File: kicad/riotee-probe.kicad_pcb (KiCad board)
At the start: 2 copper layers, 43.2 x 22.9 mm, 70 parts, among them J1 12402012E212A, J2 Conn_01x05, J3 Conn_02x05_Odd_Even, J4 Conn_01x05, U1 RP2040, U2 W25Q16JVUXIQ, U3 74LVC2T45GT, U4 74LVC2T45GT, U5 74LVC2T45GT, U6 74LVC2T45GT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

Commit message: adjust values of level translator series resistors
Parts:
- R10, R11, R12, R13, R14, R15, R20, R21, R23, R24: value 120R -> 12R
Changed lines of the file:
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@@
       (effects (font (size 1 1) (thickness 0.15)))
     )
-    (fp_text value "120R" (at 0 1.17) (layer "F.Fab") hide
+    (fp_text value "12R" (at 0 1.17) (layer "F.Fab") hide
       (effects (font (size 1 1) (thickness 0.15)))
     )
@@
       (effects (font (size 1 1) (thickness 0.15)))
     )
-    (fp_text value "120R" (at 0 1.17) (layer "F.Fab") hide
+    (fp_text value "12R" (at 0 1.17) (layer "F.Fab") hide
       (effects (font (size 1 1) (thickness 0.15)))
     )
@@
       (effects (font (size 1 1) (thickness 0.15)))
     )
-    (fp_text value "120R" (at 0 1.17) (layer "F.Fab") hide
+    (fp_text value "12R" (at 0 1.17) (layer "F.Fab") hide
       (effects (font (size 1 1) (thickness 0.15)))
     )
@@
       (effects (font (size 1 1) (thickness 0.15)))
     )
-    (fp_text value "120R" (at 0 1.17) (layer "F.Fab") hide
+    (fp_text value "12R" (at 0 1.17) (layer "F.Fab") hide
       (effects (font (size 1 1) (thickness 0.15)))
     )
@@
       (effects (font (size 1 1) (thickness 0.15)))
     )
-    (fp_text value "120R" (at 0 1.17) (layer "F.Fab") hide
+    (fp_text value "12R" (at 0 1.17) (layer "F.Fab") hide
       (effects (font (size 1 1) (thickness 0.15)))
     )
@@
       (effects (font (size 1 1) (thickness 0.15)))
     )
-    (fp_text value "120R" (at 0 1.17) (layer "F.Fab") hide
+    (fp_text value "12R" (at 0 1.17) (layer "F.Fab") hide
       (effects (font (size 1 1) (thickness 0.15)))
     )
@@
       (effects (font (size 1 1) (thickness 0.15)))
     )
-    (fp_text value "120R" (at 0 1.17 90) (layer "F.Fab") hide
+    (fp_text value "12R" (at 0 1.17 90) (layer "F.Fab") hide
       (effects (font (size 1 1) (thickness 0.15)))
     )
@@
       (effects (font (size 1 1) (thickness 0.15)))
     )
-    (fp_text value "120R" (at 0 1.17) (layer "F.Fab") hide
+    (fp_text value "12R" (at 0 1.17) (layer "F.Fab") hide
       (effects (font (size 1 1) (thickness 0.15)))
     )
@@
       (effects (font (size 1 1) (thickness 0.15)))
     )
-    (fp_text value "120R" (at 0 1.17) (layer "F.Fab") hide
+    (fp_text value "12R" (at 0 1.17) (layer "F.Fab") hide
       (effects (font (size 1 1) (thickness 0.15)))
     )
@@
       (effects (font (size 1 1) (thickness 0.15)))
     )
-    (fp_text value "120R" (at 0 1.17) (layer "F.Fab") hide
+    (fp_text value "12R" (at 0 1.17) (layer "F.Fab") hide
       (effects (font (size 1 1) (thickness 0.15)))
     )

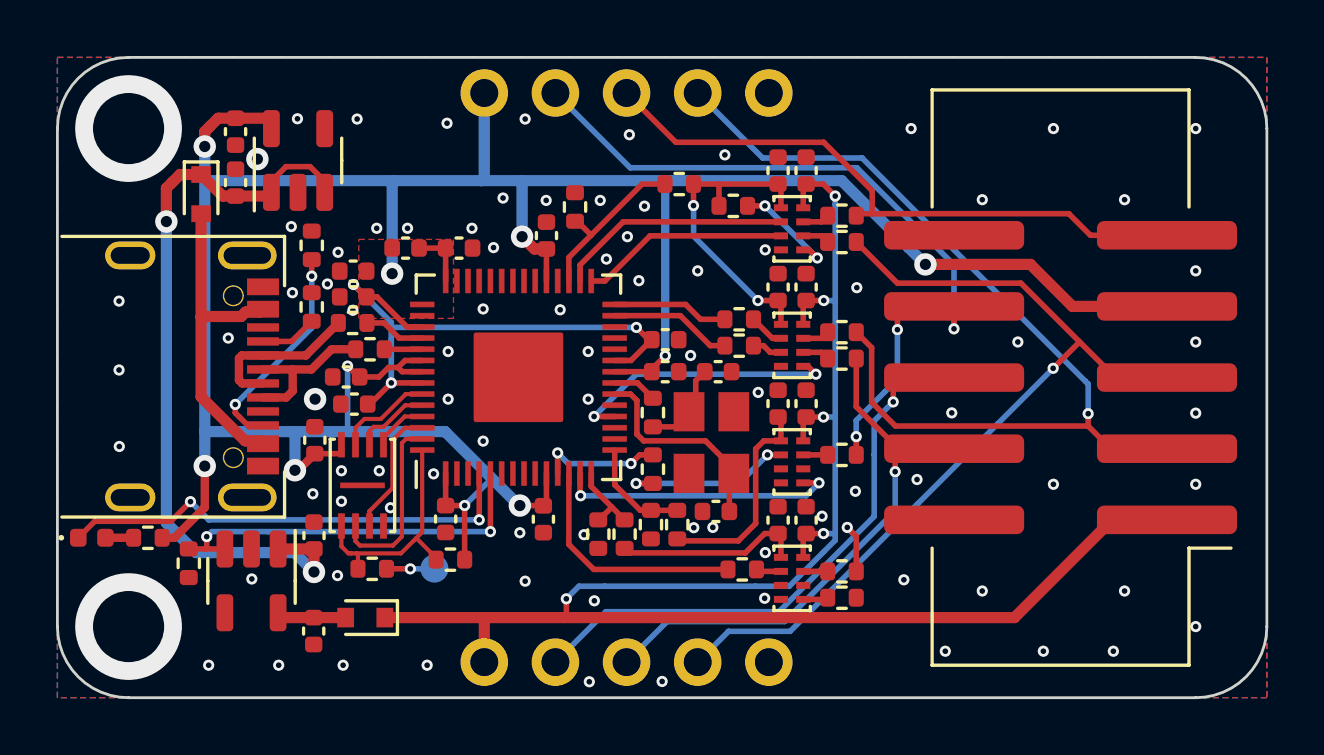
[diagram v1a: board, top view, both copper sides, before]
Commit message: replace target supply diode with analog switch
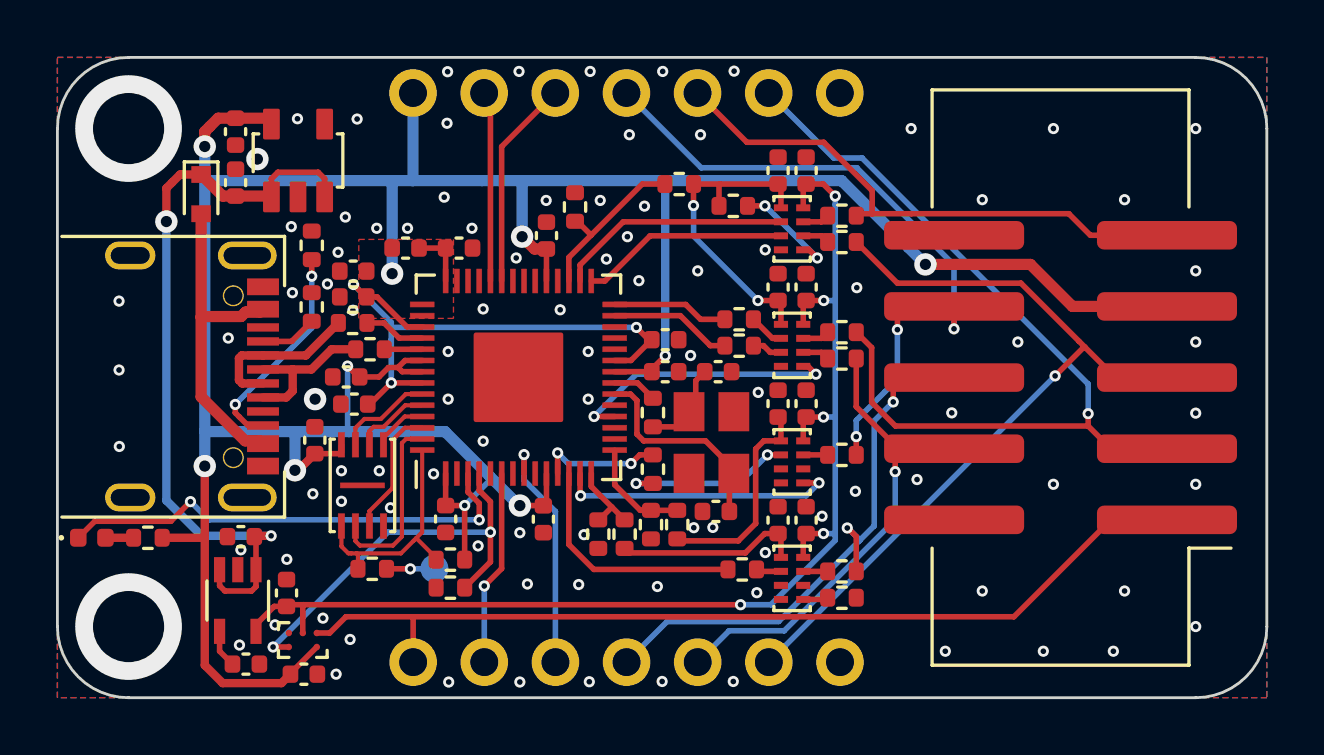
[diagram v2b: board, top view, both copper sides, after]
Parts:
- removed D3: D_Schottky, Diode_SMD:D_SOD-523
- added C25: DNP, Capacitor_SMD:C_0402_1005Metric, F.Cu at (184.5, 72.5)
- added C28: 0.1u, Capacitor_SMD:C_0402_1005Metric, F.Cu at (186.6, 72.8)
- added U9: TS5A3166YZP, riotee:TI_YZP0005, F.Cu at (186.6, 71.6)
- J2, J4: value Conn_01x05 -> Conn_01x07; footprint riotee:PinHeader_1x05_P2.54mm_Plain -> riotee:PinHeader_1x07_P2.54mm_Plain
- R27: value 5.1k -> 12R
- U7: value TLV73325PDBV -> TPS71721DCK; footprint Package_TO_SOT_SMD:SOT-23-5 -> riotee:TI_DCK0005A
- U8: footprint Package_TO_SOT_SMD:SOT-23-5 -> riotee:TI_DBV0005A
- moved R27 9.38 mm to (191.8, 69.7), turned to 0 degrees
- moved C23 2.61 mm to (184.3, 67.9), turned to 180 degrees
- moved J4 2.54 mm to (190.5, 52.1)
- moved J2 2.54 mm to (190.5, 72.4)
- moved C27 1.67 mm to (186.0, 69.9), turned to 90 degrees
- moved U7 0.85 mm to (184.2, 70.2)
- renumbered C25 to C27
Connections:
- C17 pad 1: /Connectors/TargetVcc -> +2V1
- C18 pad 1: /Connectors/TargetVcc -> +2V1
- C21 pad 1: /Connectors/TargetVcc -> +2V1
- C22 pad 1: /Connectors/TargetVcc -> +2V1
- C27 pad 1: Net-(C25-Pad1) -> +2V1
- J2 pad 2: /Connectors/Target_UART_TX -> /Connectors/PiGpio0
- J2 pad 3: /Connectors/Target_SWD.IO -> /Connectors/PiGpio1
- J2 pad 4: /Connectors/Target_SWD.CLK -> /Connectors/Target_UART_TX
- J2 pad 5: GND -> /Connectors/Target_SWD.IO
- J4 pad 2: /Connectors/Target_UART_RX -> /Connectors/PiGpio3
- J4 pad 3: /Connectors/Target_SBW.CLK -> /Connectors/PiGpio2
- J4 pad 4: /Connectors/Target_SBW.IO -> /Connectors/Target_UART_RX
- J4 pad 5: GND -> /Connectors/Target_SBW.CLK
- R27 pad 1: /Controller/TargetPowerEnable -> GND
- R27 pad 2: GND -> /Connectors/TargetPowerEnable
- U1 pad 3: unconnected-(U1-Pad3) -> /Controller/LED0
- U1 pad 37: unconnected-(U1-Pad37) -> /Connectors/PiGpio2
- U1 pad 38: unconnected-(U1-Pad38) -> /Connectors/PiGpio3
- U1 pad 4: /Controller/LED0 -> /Connectors/TargetPowerEnable
- U1 pad 5: /Controller/TargetPowerEnable -> unconnected-(U1-Pad5)
- U1 pad 6: unconnected-(U1-Pad6) -> /Connectors/PiGpio0
- U1 pad 8: unconnected-(U1-Pad8) -> /Connectors/PiGpio1
- U3 pad 8: /Connectors/TargetVcc -> +2V1
- U4 pad 8: /Connectors/TargetVcc -> +2V1
- U5 pad 8: /Connectors/TargetVcc -> +2V1
- U6 pad 8: /Connectors/TargetVcc -> +2V1
- U7 pad 3: /Controller/TargetPowerEnable -> VBUS
- U7 pad 4: unconnected-(U7-Pad4) -> Net-(C25-Pad1)
- U7 pad 5: Net-(C25-Pad1) -> +2V1
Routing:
- net +2V1: track 0.00 -> 43.4 mm, vias 0 -> 5
- net /Connectors/TargetVcc: track 62.4 -> 33.7 mm, vias 5 -> 0
- net /Connectors/TargetPowerEnable: track 0.00 -> 14.6 mm, vias 0 -> 2
- net /Controller/TargetPowerEnable: track 14.0 -> 0.00 mm, vias 2 -> 0
- net +3V3: track 105.1 -> 115.1 mm
- net /Connectors/PiGpio1: track 0.00 -> 8.55 mm, vias 0 -> 1
- net /Connectors/PiGpio2: track 0.00 -> 7.51 mm
- net /Connectors/PiGpio0: track 0.00 -> 6.99 mm, vias 0 -> 1
- net /Connectors/PiGpio3: track 0.00 -> 6.81 mm
- net /Connectors/Target_UART_RX: track 27.7 -> 25.1 mm
- net /Connectors/Target_SBW.IO: track 33.7 -> 31.2 mm
- net /Connectors/Target_SBW.CLK: track 22.5 -> 19.9 mm
- net /Connectors/Target_SWD.CLK: track 31.4 -> 29.0 mm
- net /Connectors/Target_SWD.IO: track 21.8 -> 19.5 mm
- net /Connectors/Target_UART_TX: track 22.9 -> 20.8 mm
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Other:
- board text added: "+3V3"
- board text added: "Gnd"
- board text added: "Riotee probe v0.3"
- board text added: "SbwClk"
- board text added: "SbwIo"
- board text added: "SwdClk"
- board text added: "SwdIo"
- board text added: "UartRx"
- board text added: "UartTx"
- board text added: "Vcc"
- board text removed: "Riotee probe v0.2"

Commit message: change to 4 layer board
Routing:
- added copper zone on In1.Cu, net GND
- added copper zone on In2.Cu, net GND
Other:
- copper layers 2 -> 4
- board text added: "Riotee probe v0.4"
- board text removed: "Riotee probe v0.3"
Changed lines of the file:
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@@
 (kicad_pcb (version 20211014) (generator pcbnew)
   (general
-    (thickness 1.6)
+    (thickness 1.64)
   )
   (paper "A4")
   (layers
     (0 "F.Cu" signal)
+    (1 "In1.Cu" signal)
+    (2 "In2.Cu" signal)
     (31 "B.Cu" signal)
     (32 "B.Adhes" user "B.Adhesive")
@@
       (layer "F.Mask" (type "Top Solder Mask") (thickness 0.01))
       (layer "F.Cu" (type "copper") (thickness 0.035))
-      (layer "dielectric 1" (type "core") (thickness 1.51) (material "FR4") (epsilon_r 4.5) (loss_tangent 0.02))
+      (layer "dielectric 1" (type "prepreg") (thickness 0.14) (material "FR4") (epsilon_r 4.5) (loss_tangent 0.02))
+      (layer "In1.Cu" (type "copper") (thickness 0.035))
+      (layer "dielectric 2" (type "core") (thickness 1.2) (material "FR4") (epsilon_r 4.5) (loss_tangent 0.02))
+      (layer "In2.Cu" (type "copper") (thickness 0.035))
+      (layer "dielectric 3" (type "prepreg") (thickness 0.14) (material "FR4") (epsilon_r 4.5) (loss_tangent 0.02))
       (layer "B.Cu" (type "copper") (thickness 0.035))
       (layer "B.Mask" (type "Bottom Solder Mask") (thickness 0.01))
@@
       (rotate (xyz 0 0 0))
     )
+    (model "/home/kai/workspace/Riotee_ProbeHardware/library/riotee.3dshapes/IDC-Header_2x05_P2.54mm_Vertical_SMD.step"
+      (offset (xyz 0 0 0))
+      (scale (xyz 1 1 1))
+      (rotate (xyz 0 0 0))
+    )
   )
   (footprint "riotee:PinHeader_1x07_P2.54mm_Plain" (layer "F.Cu")
@@
       (net 1 "GND") (pinfunction "SHIELD") (pintype "passive"))
     (model "${KIPRJMOD}/../library/riotee.3dshapes/AMPH_12402012E212A.step"
-      (offset (xyz 39.96 1.1 1.5))
+      (offset (xyz -0.04 -0.85 -0.325))
       (scale (xyz 1 1 1))
-      (rotate (xyz -90 0 0))
+      (rotate (xyz -0 0 0))
     )
   )
@@
     (effects (font (size 0.7 0.7) (thickness 0.15)) (justify mirror))
   )
-  (gr_text "Riotee probe v0.3" (at 193.5 63.31) (layer "B.SilkS")
+  (gr_text "Riotee probe v0.4" (at 193.5 63.31) (layer "B.SilkS")
     (effects (font (size 2 2) (thickness 0.35)) (justify mirror))
   )
@@
     )
   )
-  (zone (net 1) (net_name "GND") (layers F&B.Cu) (hatch edge 0.508)
+  (zone (net 1) (net_name "GND") (layers "F.Cu" "In1.Cu" "In2.Cu" "B.Cu") (hatch edge 0.508)
     (connect_pads thru_hole_only (clearance 0.15))
     (min_thickness 0.15) (filled_areas_thickness no)

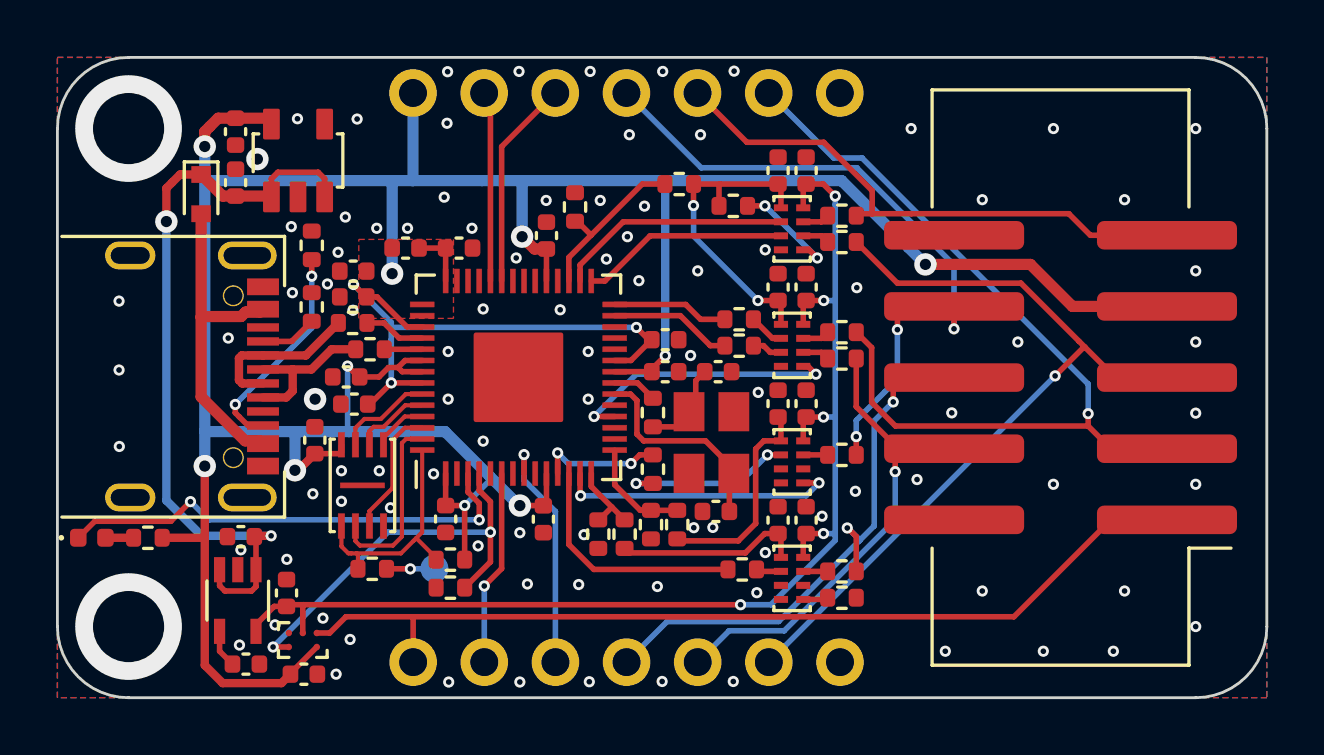
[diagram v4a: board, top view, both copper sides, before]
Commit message: update footprints and add component description to BOM
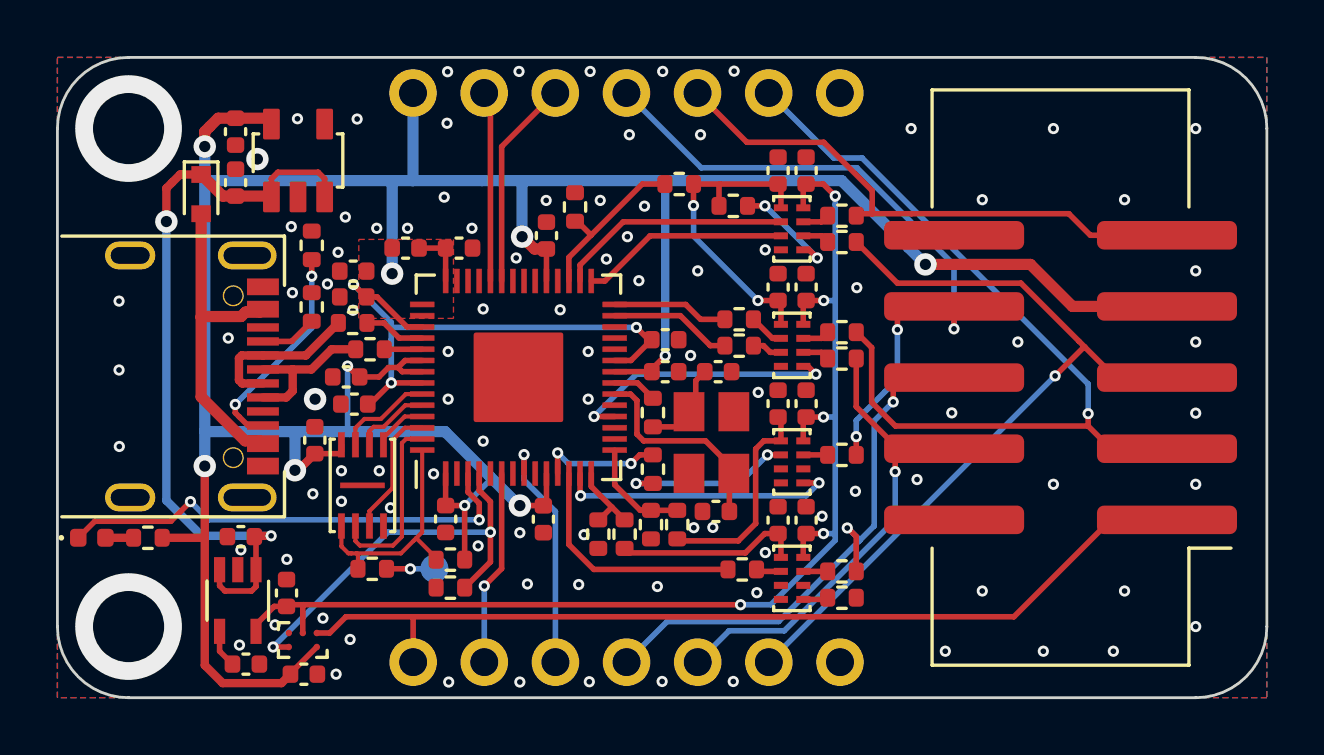
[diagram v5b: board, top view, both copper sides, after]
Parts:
- moved J1 0.24 mm to (181.7, 62.2)
- moved U5 0.07 mm to (204.0, 65.2)
- moved U4 0.07 mm to (204.0, 61.1)
- moved U3 0.07 mm to (204.0, 56.9)
- moved U6 0.07 mm to (204.0, 69.4)

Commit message: add conformity marks and refine BOM settings
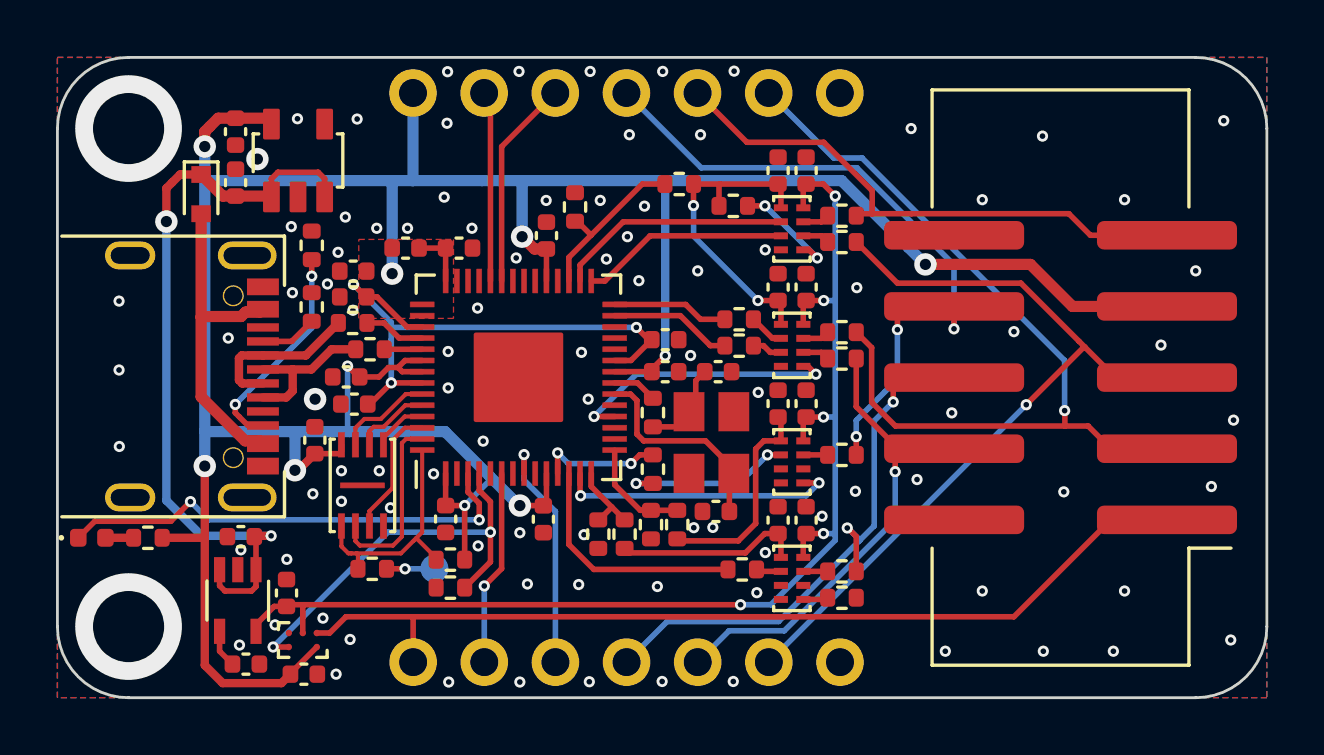
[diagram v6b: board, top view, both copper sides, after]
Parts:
- R27: value 12R -> 5.1k
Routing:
- net GND: vias 96 -> 95
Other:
- board text added: "Riotee probe v1.0"
- board text removed: "+3V3"
- board text removed: "Gnd"
- board text removed: "Riotee probe v0.4"
- board text removed: "SbwClk"
- board text removed: "SbwIo"
- board text removed: "SwdClk"
- board text removed: "SwdIo"
- board text removed: "UartRx"
- board text removed: "UartTx"
- board text removed: "Vcc"
